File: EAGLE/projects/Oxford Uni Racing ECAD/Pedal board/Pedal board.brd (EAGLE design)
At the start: 165.1 x 114 mm, 44 parts, among them IC1 AD711N, J1 ASS + BOTS, J2 THR_1_2, J3 PWR_CAN, J6 BR_POS_PRESS_STWH, K2 EC2-12TNU, T1 BT169, X2 D-SUB9-H2M09ST

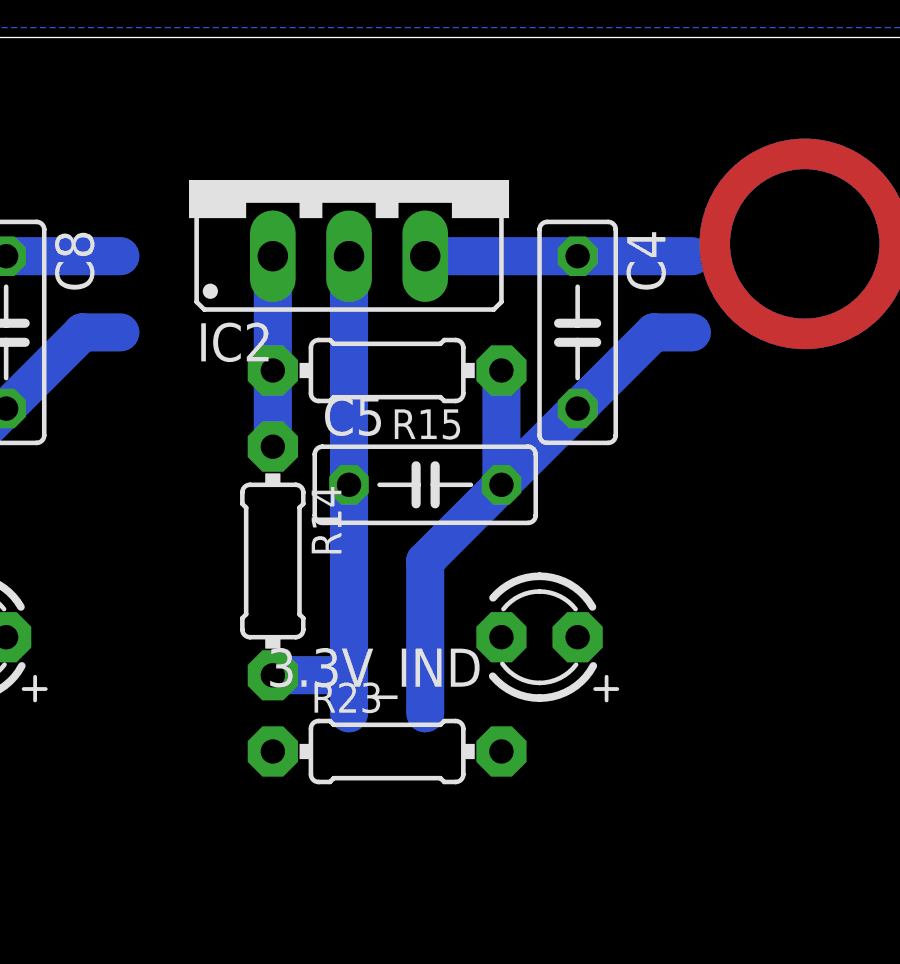
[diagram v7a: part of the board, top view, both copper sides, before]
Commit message: removed 3.3V regulators from boards, as we will be using the onbloard regulator
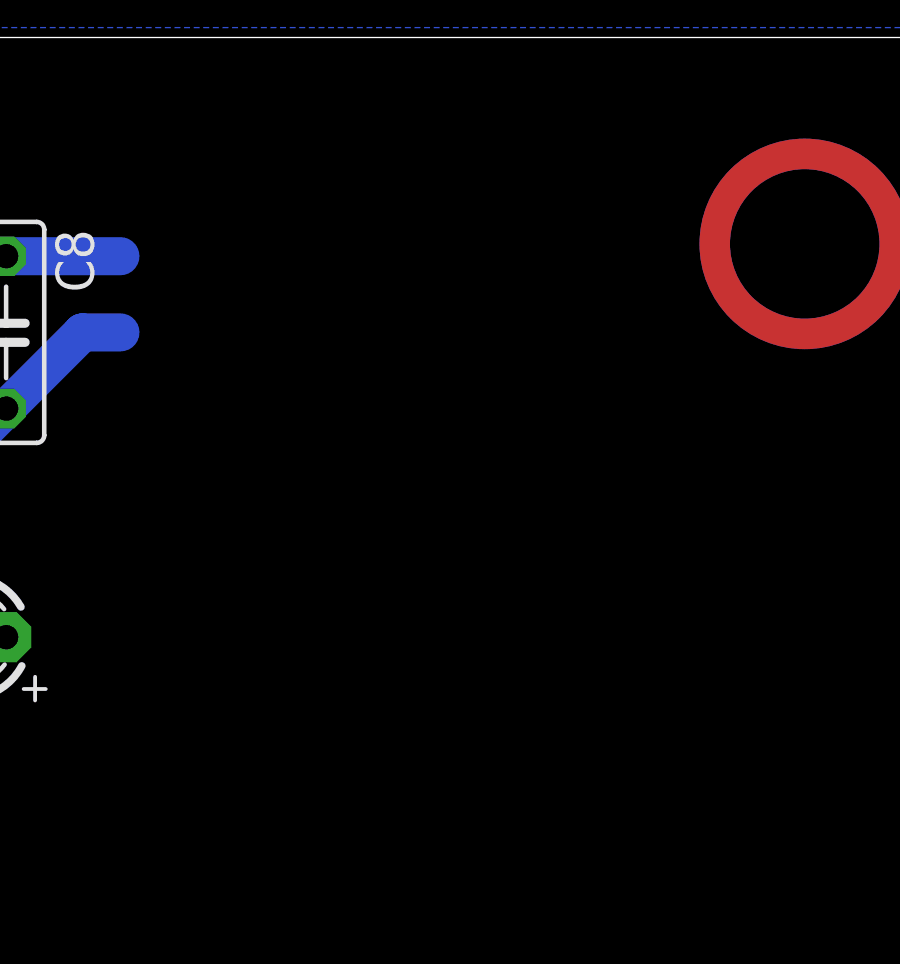
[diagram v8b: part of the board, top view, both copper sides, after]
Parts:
- removed 3.3V_IND: (no value), adafruit:LED3MM
- removed C4: 0.1uF, adafruit:C050-025X075
- removed C5: 1uF, adafruit:C050-025X075
- removed IC2: (no value), v-reg:317TS
- removed R14: 240, adafruit:0204/7
- removed R15: 390, adafruit:0204/7
- removed R23: (no value), adafruit:0204/7
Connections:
- removed net N$12: 3.3V_IND.K, R23.2
- removed net N$24: IC2.1, R14.1, R15.2
- net 12V: no longer C4.1, IC2.3
- net 3.3V: now also U$1.J802-3; no longer 3.3V_IND.A, C5.1, IC2.2, R14.2
- net GND: no longer C4.2, C5.2, R15.1, R23.1
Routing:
- net GND: track 189.0 -> 168.1 mm
- net 3.3V: track 17.8 -> 0.00 mm
- net 12V: track 183.5 -> 174.6 mm
- net N$24: track 6.35 -> 0.00 mm
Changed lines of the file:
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@@
 <attribute name="VALUE" x="91.44" y="88.9" size="1.27" layer="27" align="center"/>
-</element>
-<element name="IC2" library="v-reg" library_urn="urn:adsk.eagle:library:409" package="317TS" package3d_urn="urn:adsk.eagle:package:30353/1" value="" x="142.24" y="109.22" smashed="yes">
-<attribute name="NAME" x="137.16" y="103.1748" size="1.27" layer="25" ratio="10"/>
-<attribute name="VALUE" x="137.16" y="101.6" size="1.27" layer="27" ratio="10"/>
-</element>
-<element name="R14" library="adafruit" library_urn="urn:adsk.eagle:library:420" package="0204/7" package3d_urn="urn:adsk.eagle:package:6240596/1" value="240" x="139.7" y="96.52" smashed="yes" rot="R270">
-<attribute name="NAME" x="140.9954" y="99.06" size="0.9906" layer="25" ratio="12" rot="R270"/>
-<attribute name="VALUE" x="139.2174" y="98.1456" size="0.9906" layer="27" ratio="12" rot="R270"/>
-</element>
-<element name="R15" library="adafruit" library_urn="urn:adsk.eagle:library:420" package="0204/7" package3d_urn="urn:adsk.eagle:package:6240596/1" value="390" x="143.51" y="102.87" smashed="yes" rot="R180">
-<attribute name="NAME" x="146.05" y="101.5746" size="0.9906" layer="25" ratio="12" rot="R180"/>
-<attribute name="VALUE" x="145.1356" y="103.3526" size="0.9906" layer="27" ratio="12" rot="R180"/>
-</element>
-<element name="C4" library="adafruit" library_urn="urn:adsk.eagle:library:420" package="C050-025X075" package3d_urn="urn:adsk.eagle:package:6240357/1" value="0.1uF" x="149.86" y="104.14" smashed="yes" rot="R270">
-<attribute name="NAME" x="151.511" y="107.569" size="1.27" layer="25" ratio="10" rot="R270"/>
-<attribute name="VALUE" x="147.066" y="107.569" size="1.27" layer="27" ratio="10" rot="R270"/>
-</element>
-<element name="C5" library="adafruit" library_urn="urn:adsk.eagle:library:420" package="C050-025X075" package3d_urn="urn:adsk.eagle:package:6240357/1" value="1uF" x="144.78" y="99.06" smashed="yes">
-<attribute name="NAME" x="141.351" y="100.711" size="1.27" layer="25" ratio="10"/>
-<attribute name="VALUE" x="141.351" y="96.266" size="1.27" layer="27" ratio="10"/>
 </element>
 <element name="IC4" library="v-reg" library_urn="urn:adsk.eagle:library:409" package="317TS" package3d_urn="urn:adsk.eagle:package:30353/1" value="" x="123.19" y="109.22" smashed="yes">
@@
 <attribute name="NAME" x="106.68" y="24.1046" size="0.9906" layer="25" ratio="12" rot="R180"/>
 <attribute name="VALUE" x="105.7656" y="25.8826" size="0.9906" layer="27" ratio="12" rot="R180"/>
-</element>
-<element name="3.3V_IND" library="adafruit" library_urn="urn:adsk.eagle:library:420" package="LED3MM" package3d_urn="urn:adsk.eagle:package:6240537/1" value="" x="148.59" y="93.98" smashed="yes" rot="R180">
-<attribute name="NAME" x="146.685" y="93.599" size="1.27" layer="25" ratio="10" rot="R180"/>
-<attribute name="VALUE" x="146.685" y="95.631" size="1.27" layer="27" ratio="10" rot="R180"/>
-</element>
-<element name="R23" library="adafruit" library_urn="urn:adsk.eagle:library:420" package="0204/7" package3d_urn="urn:adsk.eagle:package:6240596/1" value="" x="143.51" y="90.17" smashed="yes">
-<attribute name="NAME" x="140.97" y="91.4654" size="0.9906" layer="25" ratio="12"/>
-<attribute name="VALUE" x="141.8844" y="89.6874" size="0.9906" layer="27" ratio="12"/>
 </element>
 <element name="5V_IND" library="adafruit" library_urn="urn:adsk.eagle:library:420" package="LED3MM" package3d_urn="urn:adsk.eagle:package:6240537/1" value="" x="129.54" y="93.98" smashed="yes" rot="R180">
@@
 <vertex x="165.1" y="114.3"/>
 </polygon>
-<contactref element="C4" pad="2"/>
-<contactref element="R15" pad="1"/>
-<contactref element="C5" pad="2"/>
-<wire x1="149.86" y1="101.6" x2="152.4" y2="104.14" width="1.27" layer="16"/>
-<wire x1="152.4" y1="104.14" x2="153.67" y2="104.14" width="1.27" layer="16"/>
-<wire x1="149.86" y1="101.6" x2="147.32" y2="99.06" width="1.27" layer="16"/>
-<wire x1="147.32" y1="102.87" x2="147.32" y2="99.06" width="1.27" layer="16"/>
-<wire x1="147.32" y1="99.06" x2="144.78" y2="96.52" width="1.27" layer="16"/>
-<wire x1="144.78" y1="96.52" x2="144.78" y2="91.44" width="1.27" layer="16"/>
 <contactref element="C8" pad="2"/>
 <contactref element="R19" pad="1"/>
@@
 <wire x1="182.88" y1="29.21" x2="186.18835" y2="29.21" width="0.8128" layer="16"/>
 <contactref element="R24" pad="1"/>
-<contactref element="R23" pad="1"/>
 <contactref element="U$1" pad="J802-5"/>
 <contactref element="U$1" pad="J802-6"/>
@@
 <wire x1="186.18835" y1="29.21" x2="188.01714375" y2="26.57855625" width="0" layer="19" extent="16-16"/>
 <wire x1="182.88" y1="32.5657875" x2="182.88" y2="29.21" width="0" layer="19" extent="16-16"/>
-<wire x1="144.78" y1="91.44" x2="180.161775" y2="42.920925" width="0" layer="19" extent="16-16"/>
-<wire x1="139.7" y1="90.17" x2="144.78" y2="91.44" width="0" layer="19" extent="16-16"/>
-<wire x1="134.62" y1="104.14" x2="144.78" y2="96.52" width="0" layer="19" extent="16-16"/>
-<wire x1="120.65" y1="90.17" x2="125.73" y2="91.44" width="0" layer="19" extent="16-16"/>
-<wire x1="99.06" y1="105.5624" x2="120.65" y2="90.17" width="0" layer="19" extent="1-1"/>
-<wire x1="87.63" y1="69.85" x2="93.98" y2="91.44" width="0" layer="19" extent="1-1"/>
-<wire x1="87.63" y1="62.23" x2="87.63" y2="69.85" width="0" layer="19" extent="1-1"/>
-<wire x1="87.63" y1="46.99" x2="87.63" y2="62.23" width="0" layer="19" extent="1-1"/>
+<wire x1="109.22" y1="30.48" x2="179.202075" y2="36.2437125" width="0" layer="19" extent="16-16"/>
+<wire x1="105.41" y1="31.75" x2="109.22" y2="30.48" width="0" layer="19" extent="1-1"/>
+<wire x1="87.63" y1="26.67" x2="105.41" y2="31.75" width="0" layer="19" extent="1-1"/>
+<wire x1="87.63" y1="46.99" x2="87.63" y2="26.67" width="0" layer="19" extent="1-1"/>
 <wire x1="90.17" y1="46.99" x2="87.63" y2="46.99" width="0" layer="19" extent="1-1"/>
-<wire x1="87.63" y1="26.67" x2="87.63" y2="46.99" width="0" layer="19" extent="1-1"/>
-<wire x1="105.41" y1="31.75" x2="87.63" y2="26.67" width="0" layer="19" extent="1-1"/>
-<wire x1="109.22" y1="30.48" x2="105.41" y2="31.75" width="0" layer="19" extent="1-1"/>
+<wire x1="87.63" y1="62.23" x2="87.63" y2="46.99" width="0" layer="19" extent="1-1"/>
+<wire x1="87.63" y1="69.85" x2="87.63" y2="62.23" width="0" layer="19" extent="1-1"/>
+<wire x1="93.98" y1="91.44" x2="87.63" y2="69.85" width="0" layer="19" extent="1-1"/>
 <wire x1="63.5" y1="60.96" x2="87.63" y2="62.23" width="0" layer="19" extent="1-1"/>
 <wire x1="63.5" y1="58.42" x2="63.5" y2="60.96" width="0" layer="19" extent="1-1"/>
+<wire x1="120.65" y1="90.17" x2="99.06" y2="105.5624" width="0" layer="19" extent="1-1"/>
+<wire x1="125.73" y1="91.44" x2="120.65" y2="90.17" width="0" layer="19" extent="16-16"/>
 </signal>
 <signal name="N$7">
@@
 <wire x1="226.144503125" y1="22.298659375" x2="223.865440625" y2="24.577721875" width="0.8128" layer="16"/>
 <wire x1="202.569446875" y1="17.4301125" x2="202.569446875" y2="17.14055625" width="0.8128" layer="16"/>
-<contactref element="IC2" pad="3"/>
-<contactref element="C4" pad="1"/>
-<wire x1="144.78" y1="106.68" x2="149.86" y2="106.68" width="1.27" layer="16"/>
-<wire x1="149.86" y1="106.68" x2="153.67" y2="106.68" width="1.27" layer="16"/>
 <contactref element="IC4" pad="3"/>
 <contactref element="C8" pad="1"/>
@@
 <wire x1="113.03" y1="92.71" x2="115.67" y2="67.035" width="0" layer="19" extent="1-1"/>
 <wire x1="125.73" y1="106.68" x2="113.03" y2="92.71" width="0" layer="19" extent="1-1"/>
-<wire x1="144.78" y1="106.68" x2="134.62" y2="106.68" width="0" layer="19" extent="16-16"/>
 </signal>
 <signal name="CANL">
@@
 <wire x1="103.2129" y1="102.7176" x2="120.65" y2="92.71" width="0" layer="19" extent="1-1"/>
 </signal>
-<signal name="N$24">
-<contactref element="IC2" pad="1"/>
-<contactref element="R15" pad="2"/>
-<contactref element="R14" pad="1"/>
-<wire x1="139.7" y1="106.68" x2="139.7" y2="102.87" width="1.27" layer="16"/>
-<wire x1="139.7" y1="100.33" x2="139.7" y2="102.87" width="1.27" layer="16"/>
-</signal>
 <signal name="N$26">
 <contactref element="IC4" pad="1"/>
@@
 </signal>
 <signal name="3.3V">
-<contactref element="IC2" pad="2"/>
-<contactref element="C5" pad="1"/>
-<contactref element="R14" pad="2"/>
-<wire x1="142.24" y1="106.68" x2="142.24" y2="99.06" width="1.27" layer="16"/>
-<wire x1="142.24" y1="99.06" x2="142.24" y2="92.71" width="1.27" layer="16"/>
-<wire x1="142.24" y1="92.71" x2="142.24" y2="91.44" width="1.27" layer="16"/>
-<wire x1="139.7" y1="92.71" x2="142.24" y2="92.71" width="1.27" layer="16"/>
 <contactref element="J6" pad="1"/>
-<contactref element="3.3V_IND" pad="A"/>
-<wire x1="142.24" y1="92.71" x2="149.86" y2="93.98" width="0" layer="19" extent="16-16"/>
-<wire x1="87.63" y1="29.21" x2="139.7" y2="92.71" width="0" layer="19" extent="1-1"/>
+<contactref element="U$1" pad="J802-3"/>
+<wire x1="87.63" y1="29.21" x2="63.5" y2="66.04" width="0" layer="19" extent="1-1"/>
 </signal>
 <signal name="BR_POSS">
@@
 <wire x1="128.27" y1="90.17" x2="128.27" y2="93.98" width="0" layer="19" extent="1-1"/>
 </signal>
-<signal name="N$12">
-<contactref element="R23" pad="2"/>
-<contactref element="3.3V_IND" pad="K"/>
-<wire x1="147.32" y1="90.17" x2="147.32" y2="93.98" width="0" layer="19" extent="1-1"/>
-</signal>
 </signals>
